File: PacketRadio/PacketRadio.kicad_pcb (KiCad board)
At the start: 2 copper layers, 58 x 34 mm, 70 parts, among them J5 USB_B_Micro, Q1 BC847, Q2 BC857, U1 PCM2912APJT, U2 FT232RL, U3 XR22404CG28-F, Y1 6 MHz, Y3 12 MHz

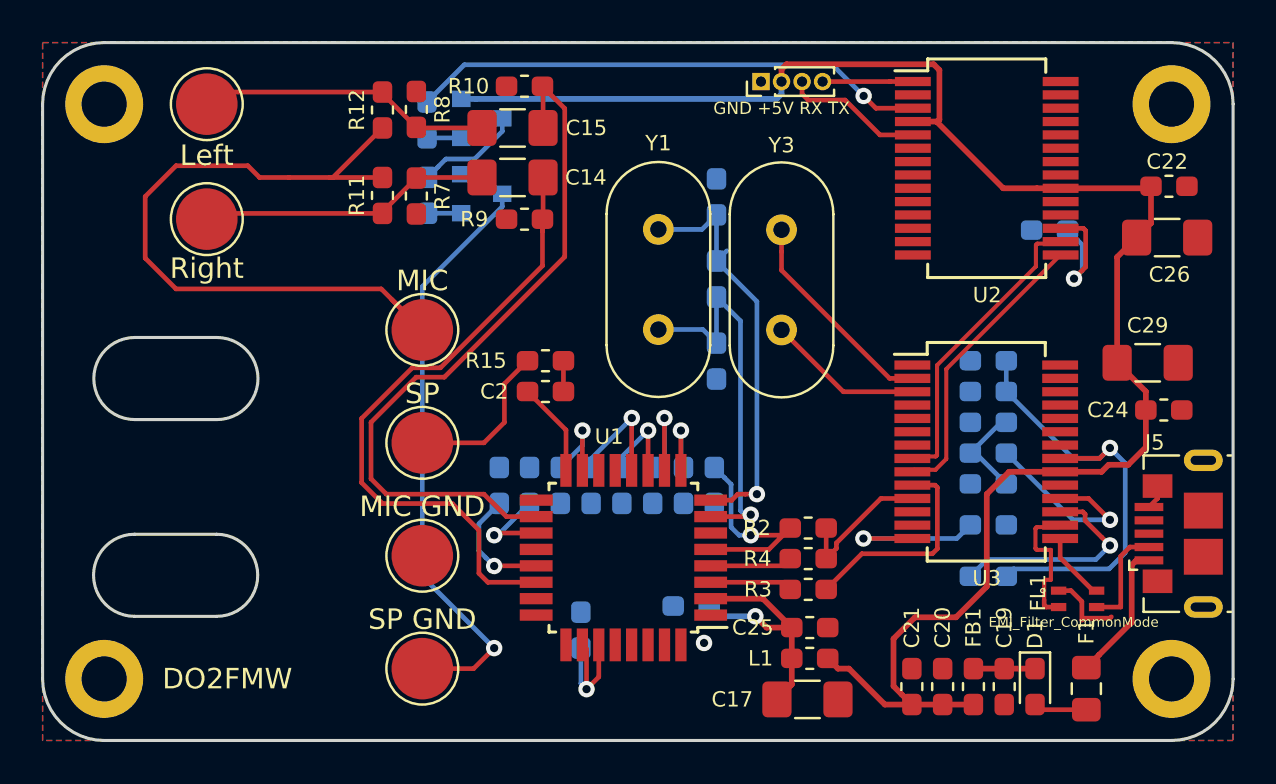
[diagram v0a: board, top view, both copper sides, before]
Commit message: Add common mode choke
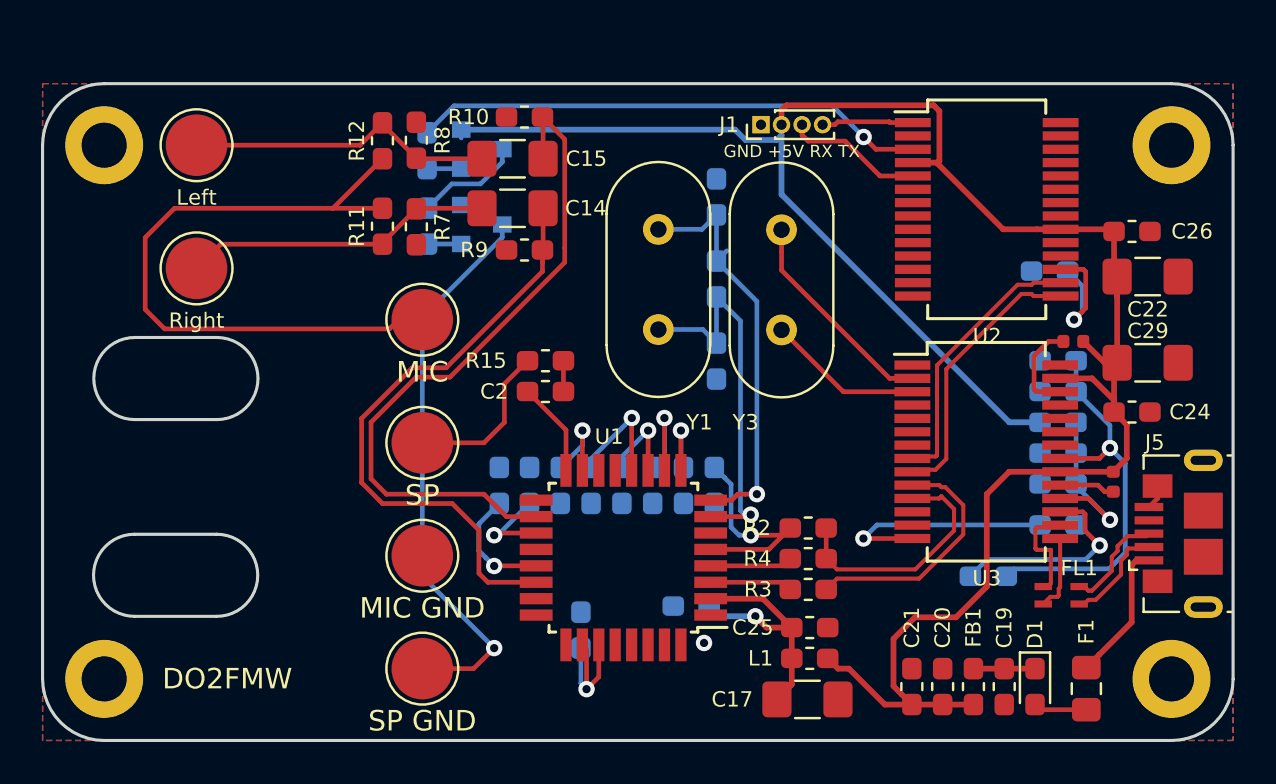
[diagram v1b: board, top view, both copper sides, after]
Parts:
- removed GND +5V RX TX: UART Connector, Connector_PinHeader_1.00mm:PinHeader_1x04_P1.00mm_Vertical
- removed Left: Left, TestPoint:TestPoint_Pad_D3.0mm
- removed MIC: MIC, TestPoint:TestPoint_Pad_D3.0mm
- removed MIC GND: MIC_GND, TestPoint:TestPoint_Pad_D3.0mm
- removed REF**: OSHW-Logo2_14.6x12mm_SilkScreen, Symbol:OSHW-Logo2_14.6x12mm_SilkScreen
- removed Right: Right, TestPoint:TestPoint_Pad_D3.0mm
- removed SP: SP, TestPoint:TestPoint_Pad_D3.0mm
- removed SP GND: SP_GND, TestPoint:TestPoint_Pad_D3.0mm
- added J1: GND +5V RX TX, Connector_PinHeader_1.00mm:PinHeader_1x04_P1.00mm_Vertical, F.Cu at (232.7, 74.5)
- added R16: 0, Resistor_SMD:R_0402_1005Metric, F.Cu at (249.8, 91.9)
- added R18: 0, Resistor_SMD:R_0402_1005Metric, F.Cu at (247.9, 85.1)
- added TP1: Right, TestPoint:TestPoint_Pad_D3.0mm, F.Cu at (205.2, 81.5)
- added TP2: Left, TestPoint:TestPoint_Pad_D3.0mm, F.Cu at (205.2, 75.5)
- added TP3: SP GND, TestPoint:TestPoint_Pad_D3.0mm, F.Cu at (216.2, 101.0)
- added TP4: MIC GND, TestPoint:TestPoint_Pad_D3.0mm, F.Cu at (216.2, 95.5)
- added TP5: MIC, TestPoint:TestPoint_Pad_D3.0mm, F.Cu at (216.2, 84.0)
- added TP6: SP, TestPoint:TestPoint_Pad_D3.0mm, F.Cu at (216.2, 90.0)
- FL1: footprint ACM2012-201-2P-T001:FIL_ACM2012-201-2P-T001 -> we-common-mode:WE-CNSW-HF
- moved C27 3.72 mm to (247.2, 90.5)
- moved R13 3.71 mm to (247.1, 89.0)
- moved C18 3.40 mm to (247.2, 86.0)
- moved C23 3.40 mm to (247.2, 87.5)
- moved R14 3.40 mm to (247.2, 92.0)
- moved R6 3.40 mm to (247.2, 94.0)
- moved C26 2.84 mm to (250.8, 79.7)
- moved C22 2.12 mm to (251.5, 81.9)
- moved C16 2.00 mm to (246.7, 81.7)
- moved H2 2.00 mm to (200.7, 75.5)
- moved H3 2.00 mm to (252.7, 75.5)
- moved U2 2.00 mm to (243.7, 78.6)
- moved C24 1.55 mm to (250.8, 88.5)
- moved C14 1.50 mm to (220.6, 78.6)
- moved C15 1.50 mm to (220.6, 76.2)
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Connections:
- net Net-(R3-Pad2) renamed /USB_SC_R_N
- net Net-(R4-Pad2) renamed /USB_SC_R_P
- FL1 pad 1: Net-(FL1-Pad1) -> USB_P
- FL1 pad 2: USB_P -> /D_P
- FL1 pad 3: Net-(FL1-Pad3) -> USB_N
- FL1 pad 4: USB_N -> /D_N
- J5 pad 2: Net-(FL1-Pad3) -> /D_N
- J5 pad 3: Net-(FL1-Pad1) -> /D_P
- R13 pad 1: Net-(C27-Pad2) -> VBUS
- R13 pad 2: Net-(R13-Pad2) -> Net-(C27-Pad2)
- U3 pad 18: Net-(R13-Pad2) -> Net-(C27-Pad2)
- U3 pad 19: BGND -> Net-(R16-Pad1)
- U3 pad 26: (no net) -> Net-(R18-Pad2)
- U3 pad 27: BGND -> VBUS
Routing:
- net VBUS: track 85.4 -> 105.5 mm
- net Net-(R13-Pad2): track 9.25 -> 0.00 mm, vias 1 -> 0
- net Net-(FL1-Pad3): track 5.21 -> 0.00 mm
- net /D_P: track 0.00 -> 5.17 mm
- net /D_N: track 0.00 -> 5.09 mm
- net USB_SC_P: track 7.06 -> 12.1 mm
- net Net-(R18-Pad2): track 0.00 -> 4.67 mm
- net Net-(FL1-Pad1): track 3.76 -> 0.00 mm
- net Net-(C27-Pad2): track 4.74 -> 8.29 mm, vias 0 -> 1
- net MIC: track 36.5 -> 33.1 mm
- net Net-(R6-Pad2): track 7.96 -> 11.4 mm
- net VCC33: track 22.4 -> 19.3 mm
- net Net-(R16-Pad1): track 0.00 -> 2.72 mm
- net USB_P: track 6.75 -> 5.09 mm
- net USB_SC_N: track 10.5 -> 12.1 mm
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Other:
- board size 58 x 34 mm -> 58 x 32 mm
- board text added: "GND +5V RX TX"

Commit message: Last fixes before going into production :)
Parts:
- added REF**: OSHW-Logo2_9.8x8mm_SilkScreen, Symbol:OSHW-Logo2_9.8x8mm_SilkScreen, B.Cu at (205.2, 80.5)
- J5: footprint Connector_USB:USB_Micro-B_GCT_USB3076-30-A -> Connector_USB:USB_Micro-B_Amphenol_10103594-0001LF_Horizontal
- moved C1 1.00 mm to (224.9, 92.1)
- moved C10 1.00 mm to (222.9, 99.1)
- moved C11 1.00 mm to (228.3, 98.0)
- moved C12 1.00 mm to (218.9, 92.1)
- moved C13 1.00 mm to (220.4, 92.1)
- moved C14 1.00 mm to (219.6, 78.6)
- moved C15 1.00 mm to (219.6, 76.2)
- moved C16 1.00 mm to (245.7, 81.7)
- moved C17 1.00 mm to (233.9, 102.5)
- moved C18 1.00 mm to (246.2, 86.0)
- moved C19 1.00 mm to (243.5, 101.9)
- moved C2 1.00 mm to (221.2, 87.5)
- moved C20 1.00 mm to (240.5, 101.9)
- moved C21 1.00 mm to (239.0, 101.9)
- moved C22 1.00 mm to (250.5, 81.9)
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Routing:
- net VBUS: track 105.5 -> 124.6 mm, vias 0 -> 1
- net Net-(C15-Pad2): track 15.1 -> 13.7 mm
- net Net-(C14-Pad2): track 15.6 -> 14.2 mm
- net BGND: track 1.19 -> 0.00 mm, vias 1 -> 41
- net /D_P: track 5.17 -> 5.98 mm
- net MIC: track 33.1 -> 33.9 mm
- net /D_N: track 5.09 -> 5.85 mm
- net XTI: track 20.6 -> 19.9 mm
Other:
- rule trace_min: 0.1778 -> 0.1
